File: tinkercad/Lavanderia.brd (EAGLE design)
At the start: 68.6 x 53.3 mm, 35 parts

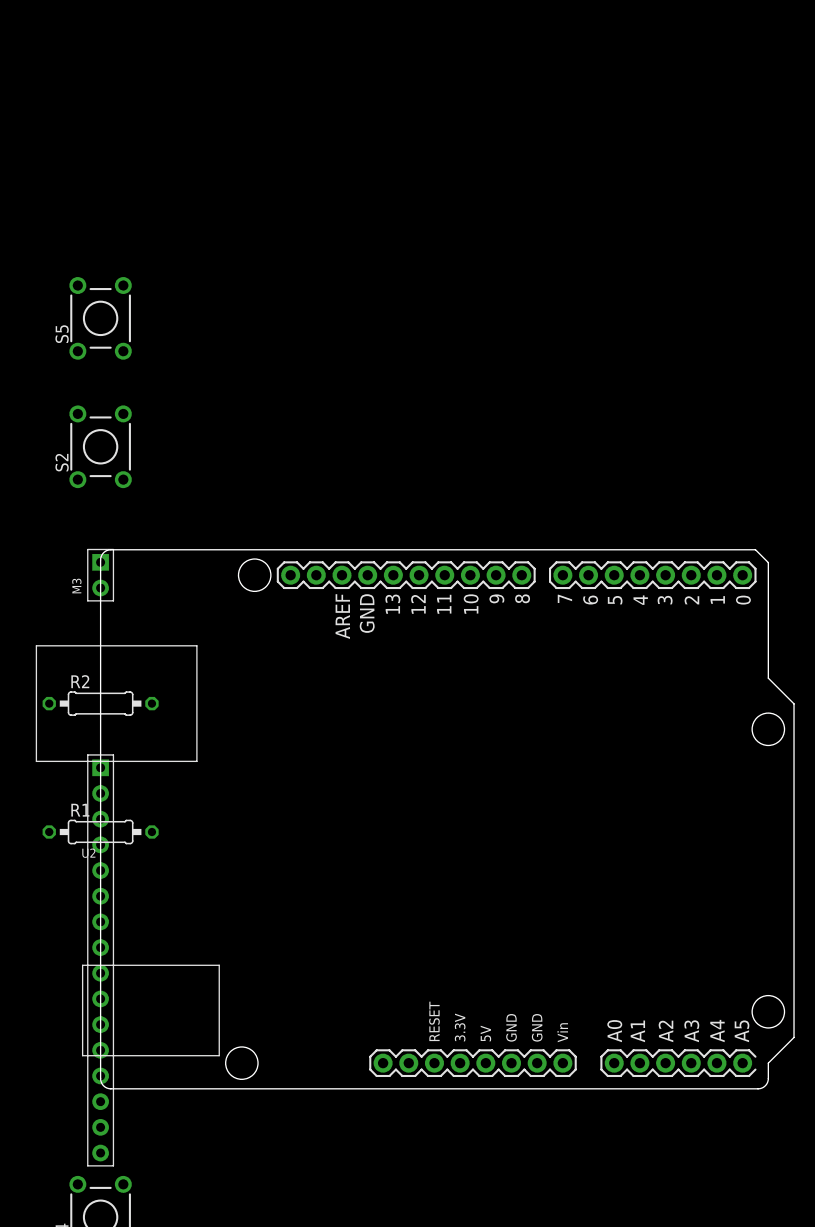
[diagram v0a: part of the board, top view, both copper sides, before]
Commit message: Atualizado Módulo de Serviços e Atendimento
Os scrips de lavagem foram alterados para seguirem o padrão do script de secagem.
Script de pagamento foi corrigido para exibir corretamente quando alugar pelo modo Lava/Seca.
Atualizado arquivo do tinkercad.
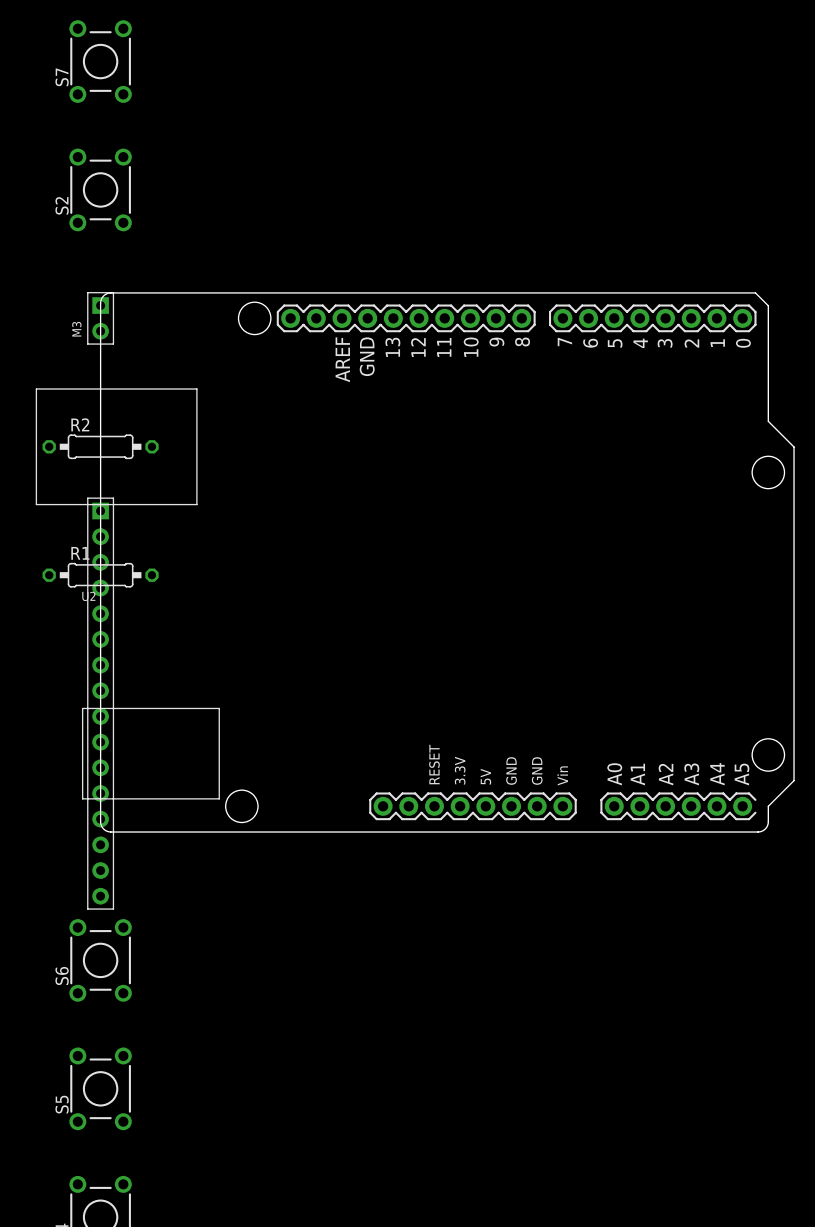
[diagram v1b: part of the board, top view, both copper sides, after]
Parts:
- UComunicador: renamed from UArduino Comunicação
- ULavadora 1: renamed from UArduino Lavador 1
- UAtendimento: renamed from UArduino Pagador
- UResidencial: renamed from UArduino Residencial
- removed UArduino Lavador 2: (no value), AUTODESK_CIRCUITS_BREADBOARD:ARDUINO_UNO
- added S6, S7: (no value), AUTODESK_CIRCUITS_BREADBOARD:TL1105
- added ULavadora 2: (no value), AUTODESK_CIRCUITS_BREADBOARD:ARDUINO_UNO
- moved S5 76.2 mm to (5.00, 365.7)
- moved M3 25.4 mm to (5.00, 441.9)
- moved R1 25.4 mm to (5.00, 416.5)
- moved R2 25.4 mm to (5.00, 429.2)
- moved S2 25.4 mm to (5.00, 454.6)
- moved U2 25.4 mm to (5.00, 403.8)
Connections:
- removed net N$1 (its old number): U4.6, ULavadora 1.3
- removed net N$16 (its old number): UArduino Lavador 2.SDA, UArduino Secador.SDA, UAtendimento.SDA, UComunicador.SDA, ULavadora 1.SDA, UResidencial.SDA
- removed net N$17 (its old number): UArduino Lavador 2.SCL, UArduino Secador.SCL, UAtendimento.SCL, UComunicador.SCL, ULavadora 1.SCL, UResidencial.SCL
- removed net N$47 (its old number): U2.4, UArduino Lavador 2.11
- removed net N$48 (its old number): U2.6, UArduino Lavador 2.3
- removed net N$49 (its old number): U2.11, UArduino Lavador 2.4
- removed net N$50 (its old number): U2.12, UArduino Lavador 2.5
- removed net N$51 (its old number): U2.13, UArduino Lavador 2.6
- removed net N$54 (its old number): R1.2, U2.1, U2.16, U2.5, UArduino Lavador 2.GND..
- new net N$59: U2.11, ULavadora 2.4
- new net N$60: U2.12, ULavadora 2.5
- new net N$61: U2.13, ULavadora 2.6
- new net N$62: U2.14, ULavadora 2.7
- new net N$63: R2.2, U2.2, ULavadora 2.5V
- new net N$64: R1.2, U2.1, U2.16, U2.5, ULavadora 2.GND..
- new net N$65: M3.2, ULavadora 2.10
- new net N$66: M3.1, ULavadora 2.GND.
- new net N$67: S2.4, ULavadora 2.2
- new net N$68: K1.2, L1.1, L2.1, M2.1, S1.3, S2.3, S3.3, S4.3, S5.3, S6.3, S7.3, SBotão Cancelar.2, SBotão OK.2, SERVO1.1, UArduino Secador.GND, UAtendimento.GND, UComunicador.GND, ULavadora 1.GND, ULavadora 2.GND, UResidencial.GND
- new net N$69: S7.4, ULavadora 2.3
- net N$52: now also U4.6, ULavadora 1.9; no longer U2.14, UArduino Lavador 2.7
- net N$53: now also S6.4, ULavadora 1.3; no longer R2.2, U2.2, UArduino Lavador 2.5V
- net N$55: now also UArduino Secador.SCL, UAtendimento.SCL, UComunicador.SCL, ULavadora 1.SCL, ULavadora 2.SCL, UResidencial.SCL; no longer M3.2, UArduino Lavador 2.10
- net N$56: now also UArduino Secador.SDA, UAtendimento.SDA, UComunicador.SDA, ULavadora 1.SDA, ULavadora 2.SDA, UResidencial.SDA; no longer M3.1, UArduino Lavador 2.GND.
- net N$57: now also U2.4, ULavadora 2.11; no longer S2.4, UArduino Lavador 2.2
- net N$58: now also U2.6, ULavadora 2.9; no longer K1.2, L1.1, L2.1, M2.1, S1.3, S2.3, S3.3, S4.3, S5.3, SBotão Cancelar.2, SBotão OK.2, SERVO1.1, UArduino Lavador 2.GND, UArduino Secador.GND, UAtendimento.GND, UComunicador.GND, ULavadora 1.GND, UResidencial.GND
